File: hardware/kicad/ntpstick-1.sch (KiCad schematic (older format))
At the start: 2 parts, among them J1 MOUNT0, J2 MOUNT1

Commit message: Version 1.2 HW design
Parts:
- added J3: MOUNT2, Walter Pin Headers:pin_strip_1, symbol HEADER_1
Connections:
- new net GND: J3.1
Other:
- note added: "Grounded mount point 4-40"
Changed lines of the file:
@@
 LIBS:max5805baub+
 LIBS:vcxo-7x5
+LIBS:lmr16006
+LIBS:tlv70xx
+LIBS:ublox-max
+LIBS:mcp4725
+LIBS:pdi-ser
 LIBS:ntpstick-1-cache
 EELAYER 25 0
@@
 encoding utf-8
 Sheet 1 3
-Title "NTP Stick 1.0"
-Date ""
+Title "NTP Stick 1.2"
+Date "Sun 29 Mar 2015"
 Rev "1"
 Comp "hairy.geek.nz"
-Comment1 "CC BY-SA"
+Comment1 "CC-NZ-3.0 BY-SA"
 Comment2 "Not Production Proven"
 Comment3 ""
@@
 F 0 "J1" H 2600 2800 60  0000 C CNN
 F 1 "MOUNT0" H 2600 2500 60  0000 C CNN
-F 2 "Walter Pin Headers:pin_strip_1" H 2600 2650 60  0000 C CNN
+F 2 "Walter Pin Headers:pin_strip_1" H 2600 2650 60  0001 C CNN
 F 3 "" H 2600 2650 60  0000 C CNN
 	1    2600 2650
@@
 F 0 "J2" H 3100 2800 60  0000 C CNN
 F 1 "MOUNT1" H 3100 2500 60  0000 C CNN
-F 2 "Walter Pin Headers:pin_strip_1" H 3100 2650 60  0000 C CNN
+F 2 "Walter Pin Headers:pin_strip_1" H 3100 2650 60  0001 C CNN
 F 3 "" H 3100 2650 60  0000 C CNN
 	1    3100 2650
@@
 NoConn ~ 2500 2650
 NoConn ~ 3200 2650
+$Comp
+L HEADER_1 J3
+U 1 1 551778B9
+P 2600 3300
+F 0 "J3" H 2600 3450 60  0000 C CNN
+F 1 "MOUNT2" H 2600 3150 60  0000 C CNN
+F 2 "Walter Pin Headers:pin_strip_1" H 2600 3300 60  0001 C CNN
+F 3 "" H 2600 3300 60  0000 C CNN
+	1    2600 3300
+	1    0    0    -1
+$EndComp
+Text Notes 2750 3350 0    60   ~ 0
+Grounded mount point 4-40
+$Comp
+L GND #PWR01
+U 1 1 55177DDF
+P 2250 3400
+F 0 "#PWR01" H 2250 3150 50  0001 C CNN
+F 1 "GND" H 2250 3250 50  0000 C CNN
+F 2 "" H 2250 3400 60  0000 C CNN
+F 3 "" H 2250 3400 60  0000 C CNN
+	1    2250 3400
+	1    0    0    -1
+$EndComp
+Wire Wire Line
+	2500 3300 2250 3300
+Wire Wire Line
+	2250 3300 2250 3400
 $EndSCHEMATC

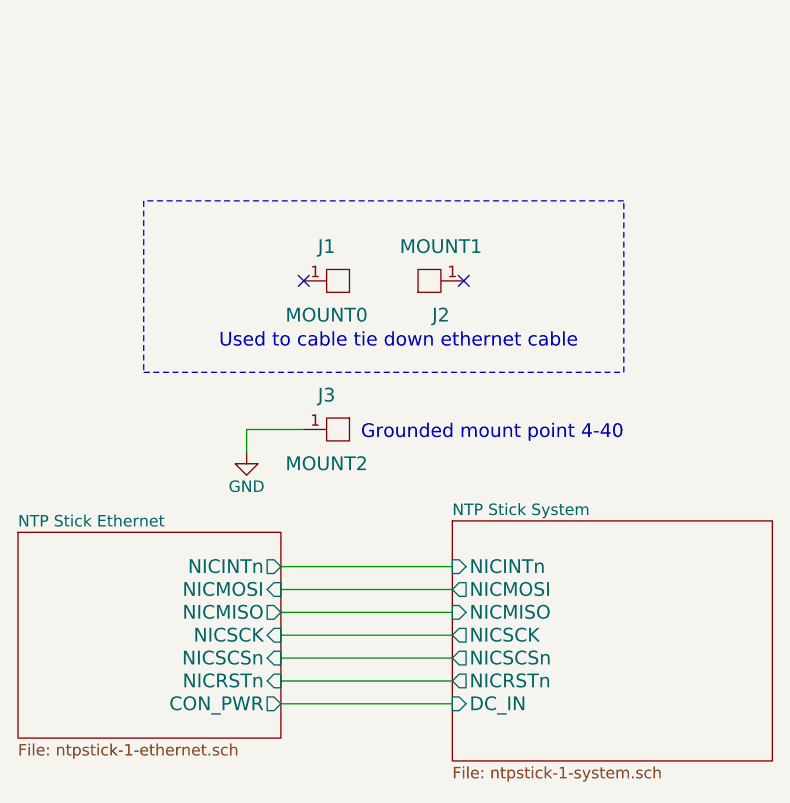
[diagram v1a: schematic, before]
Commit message: Final manufactured version of 1.2 HW
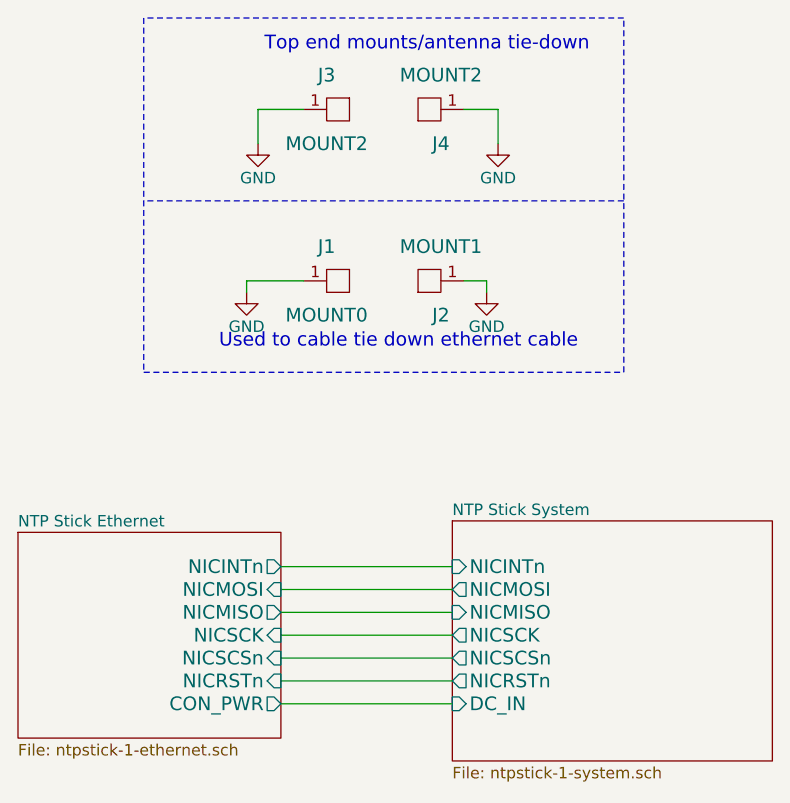
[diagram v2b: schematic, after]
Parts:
- added J4: MOUNT2, Screws:4-40-HOLE, symbol HEADER_1
- J1, J2, J3: footprint Walter Pin Headers:pin_strip_1 -> Screws:4-40-HOLE
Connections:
- net GND: now also J1.1, J2.1, J4.1
- no-connect marks 2 -> 0
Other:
- note added: "Top end mounts/antenna tie-down"
- note removed: "Grounded mount point 4-40"
- moved on the sheet: J3
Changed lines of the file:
@@
 F 0 "J1" H 2600 2800 60  0000 C CNN
 F 1 "MOUNT0" H 2600 2500 60  0000 C CNN
-F 2 "Walter Pin Headers:pin_strip_1" H 2600 2650 60  0001 C CNN
+F 2 "Screws:4-40-HOLE" H 2600 2650 60  0001 C CNN
 F 3 "" H 2600 2650 60  0000 C CNN
 	1    2600 2650
@@
 F 0 "J2" H 3100 2800 60  0000 C CNN
 F 1 "MOUNT1" H 3100 2500 60  0000 C CNN
-F 2 "Walter Pin Headers:pin_strip_1" H 3100 2650 60  0001 C CNN
+F 2 "Screws:4-40-HOLE" H 3100 2650 60  0001 C CNN
 F 3 "" H 3100 2650 60  0000 C CNN
 	1    3100 2650
@@
 Used to cable tie down ethernet cable
 Wire Notes Line
-	1800 2300 1800 3050
+	1800 1500 1800 3050
 Wire Notes Line
 	1800 3050 3900 3050
 Wire Notes Line
-	3900 3050 3900 2300
+	3900 3050 3900 1500
 Wire Notes Line
 	3900 2300 1800 2300
 Wire Wire Line
 	2400 4400 3150 4400
-NoConn ~ 2500 2650
-NoConn ~ 3200 2650
 $Comp
 L HEADER_1 J3
 U 1 1 551778B9
-P 2600 3300
-F 0 "J3" H 2600 3450 60  0000 C CNN
-F 1 "MOUNT2" H 2600 3150 60  0000 C CNN
-F 2 "Walter Pin Headers:pin_strip_1" H 2600 3300 60  0001 C CNN
-F 3 "" H 2600 3300 60  0000 C CNN
-	1    2600 3300
+P 2600 1900
+F 0 "J3" H 2600 2050 60  0000 C CNN
+F 1 "MOUNT2" H 2600 1750 60  0000 C CNN
+F 2 "Screws:4-40-HOLE" H 2600 1900 60  0001 C CNN
+F 3 "" H 2600 1900 60  0000 C CNN
+	1    2600 1900
 	1    0    0    -1
 $EndComp
-Text Notes 2750 3350 0    60   ~ 0
-Grounded mount point 4-40
 $Comp
 L GND #PWR01
 U 1 1 55177DDF
-P 2250 3400
-F 0 "#PWR01" H 2250 3150 50  0001 C CNN
-F 1 "GND" H 2250 3250 50  0000 C CNN
-F 2 "" H 2250 3400 60  0000 C CNN
-F 3 "" H 2250 3400 60  0000 C CNN
-	1    2250 3400
+P 2300 2050
+F 0 "#PWR01" H 2300 1800 50  0001 C CNN
+F 1 "GND" H 2300 1900 50  0000 C CNN
+F 2 "" H 2300 2050 60  0000 C CNN
+F 3 "" H 2300 2050 60  0000 C CNN
+	1    2300 2050
 	1    0    0    -1
 $EndComp
 Wire Wire Line
-	2500 3300 2250 3300
+	2500 2650 2250 2650
+$Comp
+L GND #PWR02
+U 1 1 55282FC9
+P 2250 2700
+F 0 "#PWR02" H 2250 2450 50  0001 C CNN
+F 1 "GND" H 2250 2550 50  0000 C CNN
+F 2 "" H 2250 2700 60  0000 C CNN
+F 3 "" H 2250 2700 60  0000 C CNN
+	1    2250 2700
+	1    0    0    -1
+$EndComp
 Wire Wire Line
-	2250 3300 2250 3400
+	2250 2650 2250 2700
+$Comp
+L GND #PWR03
+U 1 1 55283041
+P 3300 2700
+F 0 "#PWR03" H 3300 2450 50  0001 C CNN
+F 1 "GND" H 3300 2550 50  0000 C CNN
+F 2 "" H 3300 2700 60  0000 C CNN
+F 3 "" H 3300 2700 60  0000 C CNN
+	1    3300 2700
+	1    0    0    -1
+$EndComp
+Wire Wire Line
+	3200 2650 3300 2650
+Wire Wire Line
+	3300 2650 3300 2700
+$Comp
+L HEADER_1 J4
+U 1 1 55283329
+P 3100 1900
+F 0 "J4" H 3100 2050 60  0000 C CNN
+F 1 "MOUNT2" H 3100 1750 60  0000 C CNN
+F 2 "Screws:4-40-HOLE" H 3100 1900 60  0001 C CNN
+F 3 "" H 3100 1900 60  0000 C CNN
+	1    3100 1900
+	-1   0    0    1
+$EndComp
+Wire Wire Line
+	2500 1900 2300 1900
+Wire Wire Line
+	2300 1900 2300 2050
+$Comp
+L GND #PWR04
+U 1 1 55283402
+P 3350 2050
+F 0 "#PWR04" H 3350 1800 50  0001 C CNN
+F 1 "GND" H 3350 1900 50  0000 C CNN
+F 2 "" H 3350 2050 60  0000 C CNN
+F 3 "" H 3350 2050 60  0000 C CNN
+	1    3350 2050
+	1    0    0    -1
+$EndComp
+Wire Wire Line
+	3200 1900 3350 1900
+Wire Wire Line
+	3350 1900 3350 2050
+Text Notes 3750 1650 2    60   ~ 0
+Top end mounts/antenna tie-down
+Wire Notes Line
+	3900 1500 1800 1500
 $EndSCHEMATC
